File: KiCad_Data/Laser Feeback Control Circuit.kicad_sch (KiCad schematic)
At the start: 101 parts, among them P1 50k, P2 50k, SW1 SPDT Switch, P/N: 7101SD9AV2BE, SW2 SPDT Switch, P/N: 7101SD9AV2BE, SW3 SPDT Switch, P/N: 7101SD9AV2BE, SW4 SPDT Switch, P/N: 7101SD9AV2BE, SW5 SPDT Switch, P/N: 7101SD9AV2BE, SW6 SPDT Switch, P/N: 7101SD9AV2BE, SW7 SPDT Switch, P/N: 7101SD9AV2BE, T1 Transistor P/N: 2N3906, T2 Transistor P/N: 2N3906, T3 Transistor P/N: 2N3906, T4 Transistor P/N: 2N3906

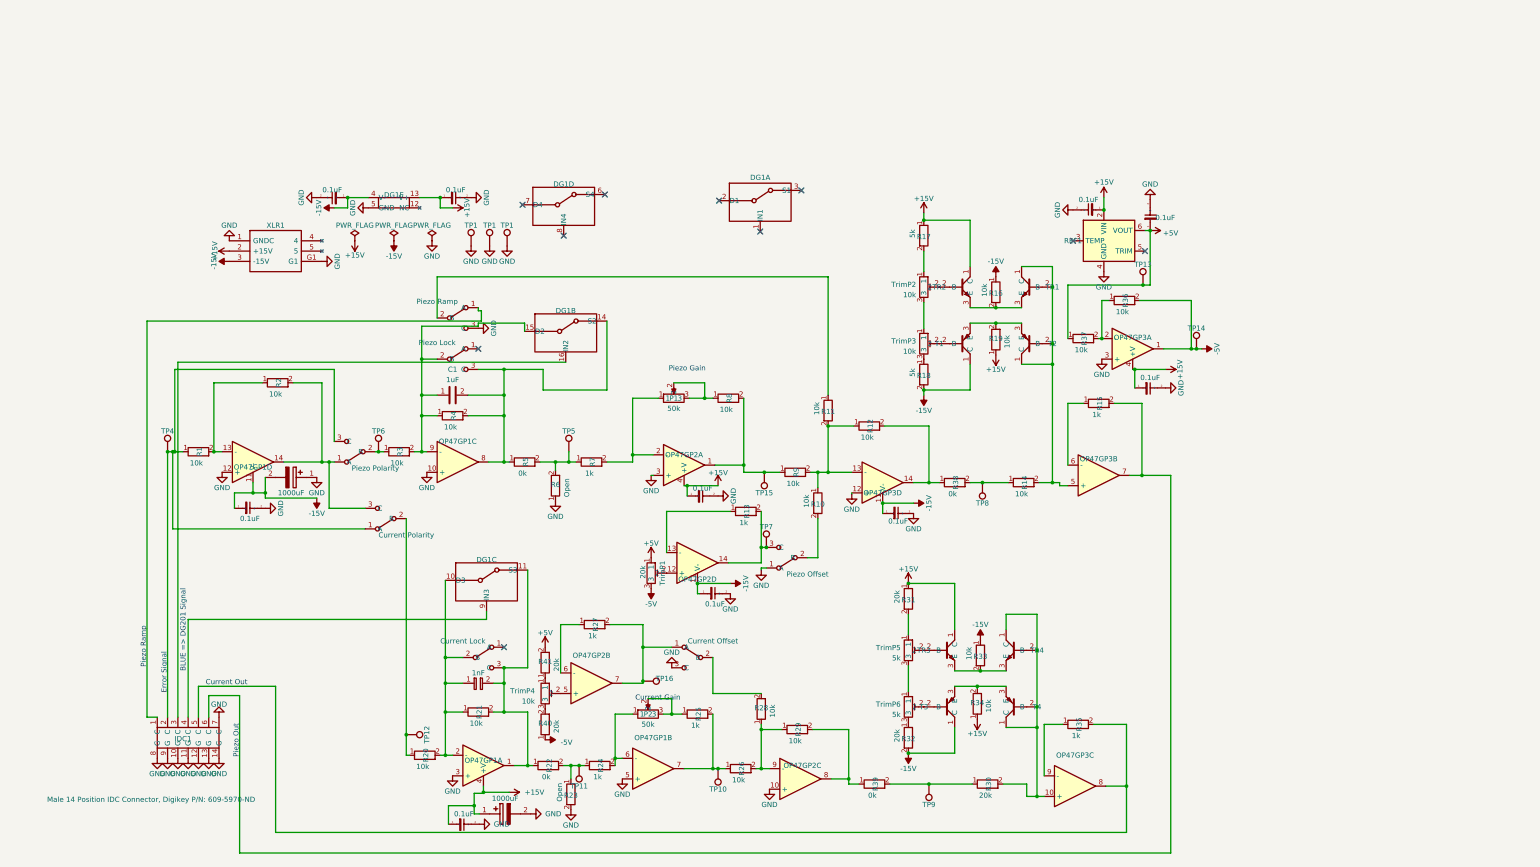
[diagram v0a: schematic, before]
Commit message: Circuit after correction
Corrections made included: 
- Using quad op-amps which reduced the space needed for the board, however, this made running traces more complicated.
- There was an error with how the IDC connector was set up in this, and all the pins had to be adjusted.
- The circuit that limited the maximum and minimum voltages at the end had a correction added where the previous version had a misconnected trace which caused the whole circuit not to function properly additionally, it was split into 2 separate components which were equivalent but did the opposite action and used to make more sense of the circuit as a whole where each was meant to make the most sense relative to what they were doing (i.e the direction the trim pot was rotated was related to the whether the voltage would decrease or increase).
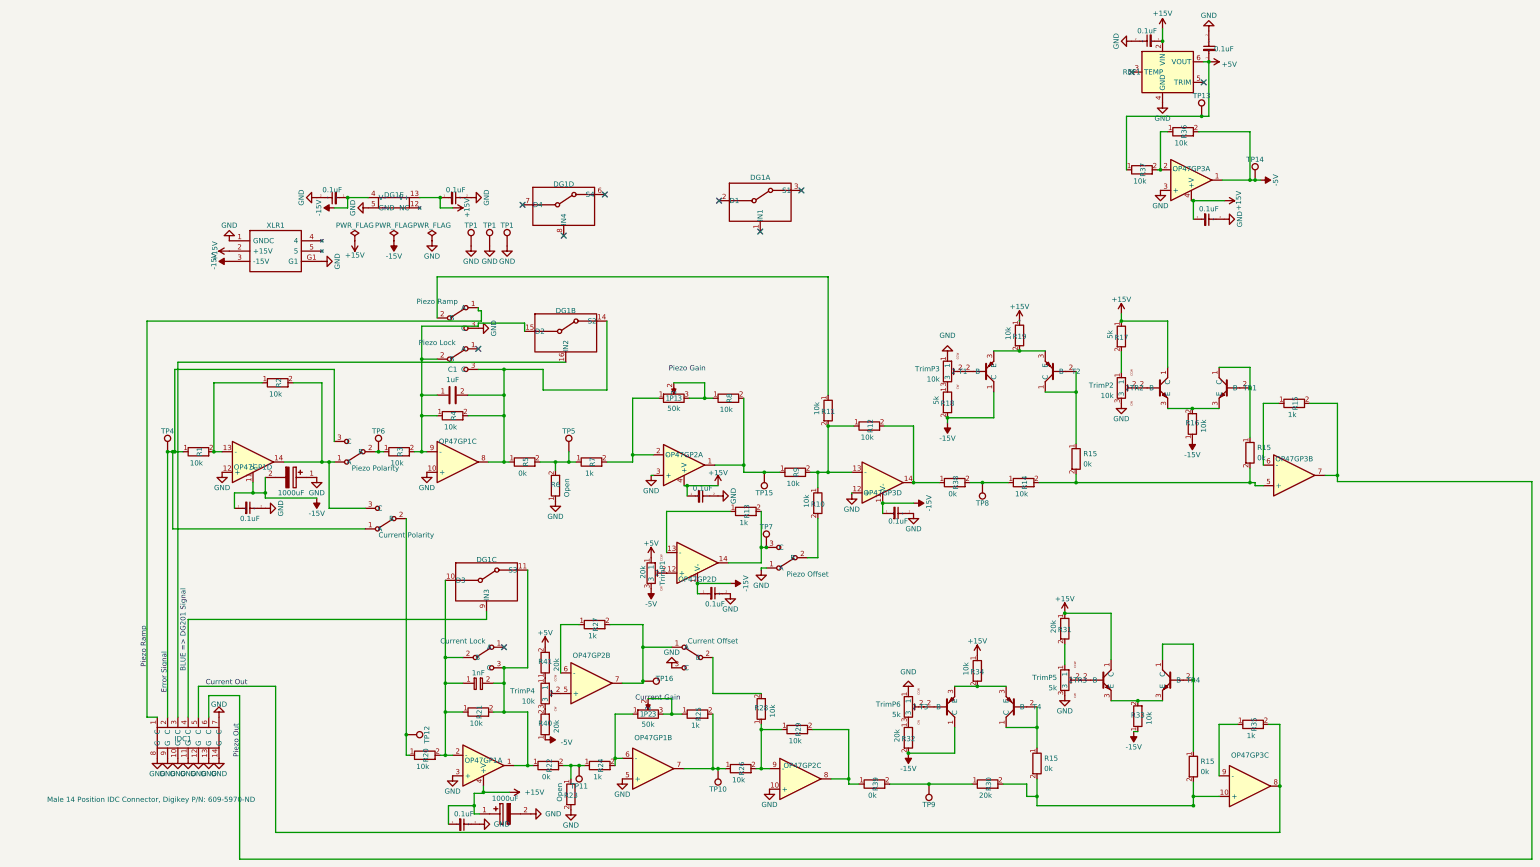
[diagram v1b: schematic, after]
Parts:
- added R15 (x4): 0k, Complex_Op_Amps_Footprints:R_Axial_DIN0207_L6.3mm_D2.5mm_P10.16mm_Horizontal, symbol Complex_Op_Amps_Footprints:Resistor
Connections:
- net GND: now also TrimP2.3, TrimP3.1, TrimP5.3, TrimP6.1
- new net: OP47GP3.5 (+), R14.2, R15.2, R15.2
- new net: R15.1, T2.1 (C), T2.2 (B)
- new net: R15.1, TR4.1 (C), TR4.2 (B)
- new net: OP47GP3.10 (+), R15.2, R15.2, R30.2
- new net: R15.1, TR1.1 (C), TR1.2 (B)
- new net: R15.1, T4.1 (C), T4.2 (B)
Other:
- moved on the sheet: OP47GP3A, OP47GP3B, OP47GP3C, R15, R18, R19, R34, R35, R36, R37, REF1, T1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
